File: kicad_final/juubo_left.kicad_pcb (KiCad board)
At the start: 2 copper layers, 145.6 x 125.5 mm, 42 parts

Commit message: Cleanup
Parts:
- removed REF** (x2): R_0201_0603, Resistor_SMD:R_0201_0603Metric_Pad0.64x0.40mm_HandSolder
- added DISP1: RES_ERJ2RKF4701X, RES_ERJ2RKF4701X, F.Cu at (209.5, 84.5)
- added DISP2: RES_ERJ2RKF4701X, RES_ERJ2RKF4701X, F.Cu at (207.6, 84.5)
- added JST1: , JST_PH_S2B-PH-K_02x2.00mm_Angled, F.Cu at (199.2, 91.1)
- added T1: , E73:SPDT_C128955, F.Cu at (199.2, 50.2)
- added _1: , MountingHole_2.2mm_M2_Pad_Via, F.Cu at (109.5, 67.6)
- added _2: , MountingHole_2.2mm_M2_Pad_Via, F.Cu at (166.7, 62.6)
- added _3: , MountingHole_2.2mm_M2_Pad_Via, F.Cu at (109.5, 105.7)
- added _4: , MountingHole_2.2mm_M2_Pad_Via, F.Cu at (177.9, 130.5)
- added _5: , MountingHole_2.2mm_M2_Pad_Via, F.Cu at (202.8, 149.3)
- added _6: , MountingHole_2.2mm_M2_Pad_Via, F.Cu at (166.7, 100.7)
- moved TRRS1 1.15 mm to (215.4, 91.7)
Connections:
- D1 pad 1: P16 -> P10
- D10 pad 1: P16 -> P10
- D11 pad 1: P14 -> P16
- D12 pad 1: P15 -> P14
- D13 pad 1: P16 -> P10
- D14 pad 1: P14 -> P16
- D15 pad 1: P15 -> P14
- D16 pad 1: P10 -> P6
- D17 pad 1: P10 -> P6
- D18 pad 1: P10 -> P6
- D2 pad 1: P14 -> P16
- D3 pad 1: P15 -> P14
- D4 pad 1: P16 -> P10
- D5 pad 1: P14 -> P16
- D6 pad 1: P15 -> P14
- D7 pad 1: P16 -> P10
- D8 pad 1: P14 -> P16
- D9 pad 1: P15 -> P14
- S1 pad 1: P18 -> P21
- S10 pad 1: P21 -> P18
- S11 pad 1: P21 -> P18
- S12 pad 1: P21 -> P18
- S13 pad 1: P1 -> P15
- S14 pad 1: P1 -> P15
- S15 pad 1: P1 -> P15
- S16 pad 1: P20 -> P19
- S17 pad 1: P21 -> P18
- S18 pad 1: P1 -> P15
- S2 pad 1: P18 -> P21
- S3 pad 1: P18 -> P21
- S4 pad 1: P19 -> P20
- S5 pad 1: P19 -> P20
- S6 pad 1: P19 -> P20
- S7 pad 1: P20 -> P19
- S8 pad 1: P20 -> P19
- S9 pad 1: P20 -> P19
- TRRS1 pad 2: P2 -> P3
- TRRS1 pad 3: P3 -> P2
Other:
- outline, holes or cut-outs redrawn
- net class Default added: clearance 0.2, trace_width 0.25, via_dia 0.8, via_drill 0.4

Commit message: Left routed
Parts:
- DISP1, DISP2: moved to B.Cu
- moved D5 11.8 mm to (107.4, 78.9)
- moved S9 11.8 mm to (126.5, 52.3)
- moved S14 11.8 mm to (164.6, 76.4)
- moved S17 11.8 mm to (184.2, 129.4)
- moved D11 11.8 mm to (145.5, 78.9)
- moved D9 11.8 mm to (126.5, 57.3)
- moved S5 11.8 mm to (107.4, 73.9)
- moved _6 11.8 mm to (155.0, 98.7)
- moved D1 11.8 mm to (88.4, 102.9)
- moved D8 11.8 mm to (126.5, 76.4)
- moved S7 11.8 mm to (126.5, 90.4)
- moved D6 11.8 mm to (107.4, 59.8)
- moved S2 11.8 mm to (88.4, 78.9)
- moved D10 11.8 mm to (145.5, 97.9)
- moved S18 11.8 mm to (201.9, 144.5)
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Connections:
- MCU1 pad 13: P1 -> VCC
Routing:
- net P15: track 0.00 -> 170.8 mm
- net P18: track 0.00 -> 170.4 mm
- net P19: track 0.00 -> 167.9 mm
- net P21: track 0.00 -> 155.2 mm
- net P10: track 0.00 -> 143.2 mm
- net P20: track 0.00 -> 136.0 mm
- net P14: track 0.00 -> 131.5 mm
- net P6: track 0.00 -> 128.9 mm
- net P16: track 0.00 -> 126.8 mm
- net GND: track 0.00 -> 116.9 mm
- net VCC: track 0.00 -> 60.1 mm, vias 0 -> 2
- net P2: track 0.00 -> 53.7 mm
- net P3: track 0.00 -> 43.1 mm
- net B+: track 0.00 -> 39.0 mm
- net RST: track 0.00 -> 33.0 mm
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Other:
- outline, holes or cut-outs redrawn
- net class Default removed

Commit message: Adjust and fix
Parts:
- moved T1 0.30 mm to (187.6, 48.4)
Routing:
- net RAW: track 5.66 -> 7.55 mm
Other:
- board size 145.6 x 125.5 mm -> 145.5 x 125.5 mm
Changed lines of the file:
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@@
   (net 40 "B+")
   (footprint "E73:SPDT_C128955" (layer "F.Cu")
-    (at 187.613786 48.115911)
+    (at 187.613786 48.4125)
     (attr through_hole)
     (fp_text reference "T1" (at 0 0) (layer "F.SilkS") hide
@@
       (net 36 "P2") (solder_mask_margin 0.102))
   )
-  (gr_arc (start 202.574223 162.941307) (mid 200.2 164) (end 197.676477 163.375839)
-    (stroke (width 0.15) (type solid)) (layer "Edge.Cuts"))
   (gr_arc (start 142.722221 109.098913) (mid 145.877217 110.612025) (end 146.634761 114.028112)
     (stroke (width 0.15) (type solid)) (layer "Edge.Cuts"))
@@
   (gr_arc (start 200.280578 47.697143) (mid 202.774498 48.99265) (end 203.800645 51.608921)
     (stroke (width 0.15) (type solid)) (layer "Edge.Cuts"))
+  (gr_line (start 202.748997 162.877717) (end 221.659673 144.499586)
+    (stroke (width 0.15) (type default)) (layer "Edge.Cuts"))
   (gr_arc (start 145.621497 129.763273) (mid 144.079016 127.892173) (end 143.900962 125.473809)
     (stroke (width 0.15) (type solid)) (layer "Edge.Cuts"))
-  (gr_arc (start 221.356718 139.908254) (mid 222.468094 142.788701) (end 221.197355 145.60246)
-    (stroke (width 0.15) (type solid)) (layer "Edge.Cuts"))
   (gr_line (start 76.838785 105.438871) (end 76.838784 51.396523)
-    (stroke (width 0.15) (type solid)) (layer "Edge.Cuts"))
-  (gr_line (start 221.197355 145.60246) (end 202.58661 162.953987)
     (stroke (width 0.15) (type solid)) (layer "Edge.Cuts"))
   (gr_line (start 79.823311 47.527571) (end 95.717823 43.355782)
@@
   (gr_line (start 143.900962 125.473809) (end 146.634761 114.028112)
     (stroke (width 0.15) (type solid)) (layer "Edge.Cuts"))
+  (gr_arc (start 202.748997 162.877717) (mid 200.311135 164.046527) (end 197.688861 163.388522)
+    (stroke (width 0.15) (type default)) (layer "Edge.Cuts"))
+  (gr_arc (start 221.356714 139.908256) (mid 222.292209 142.152188) (end 221.659673 144.499586)
+    (stroke (width 0.15) (type default)) (layer "Edge.Cuts"))
   (segment (start 191.023785 94.035912) (end 191.023785 83.040911) (width 0.25) (layer "F.Cu") (net 1))
   (segment (start 194.493785 97.505912) (end 191.023785 94.035912) (width 0.25) (layer "F.Cu") (net 1))
@@
   (segment (start 181.917187 124.803616) (end 181.404818 124.940904) (width 0.25) (layer "B.Cu") (net 31))
   (segment (start 153.589513 124.329439) (end 155.434623 125.001004) (width 0.25) (layer "B.Cu") (net 31))
+  (segment (start 181.6 51.6) (end 180.890909 50.890909) (width 0.25) (layer "B.Cu") (net 32))
+  (segment (start 185.363786 51.236214) (end 185 51.6) (width 0.25) (layer "B.Cu") (net 32))
+  (segment (start 180.890909 50.890909) (end 179.993787 50.890909) (width 0.25) (layer "B.Cu") (net 32))
   (segment (start 180.693785 50.190911) (end 179.993787 50.890909) (width 0.25) (layer "B.Cu") (net 32))
-  (segment (start 185.363786 50.190911) (end 180.693785 50.190911) (width 0.25) (layer "B.Cu") (net 32))
+  (segment (start 185 51.6) (end 181.6 51.6) (width 0.25) (layer "B.Cu") (net 32))
+  (segment (start 185.363786 50.4875) (end 185.363786 51.236214) (width 0.25) (layer "B.Cu") (net 32))
   (segment (start 202.141286 50.84591) (end 199.044757 47.749381) (width 0.25) (layer "F.Cu") (net 33))
   (segment (start 194.650619 47.749381) (end 186.429091 55.970909) (width 0.25) (layer "F.Cu") (net 33))
@@
   (segment (start 194.673785 88.548409) (end 196.8 88.548409) (width 0.25) (layer "B.Cu") (net 37))
   (segment (start 198.890909 63.590909) (end 195.233787 63.590909) (width 0.25) (layer "B.Cu") (net 37))
+  (segment (start 188.613785 89.063409) (end 188.613785 50.737499) (width 0.25) (layer "B.Cu") (net 40))
   (segment (start 188.613785 50.44091) (end 188.363786 50.190911) (width 0.25) (layer "B.Cu") (net 40))
-  (segment (start 188.613785 89.063409) (end 188.613785 50.44091) (width 0.25) (layer "B.Cu") (net 40))
+  (segment (start 188.613785 50.737499) (end 188.363786 50.4875) (width 0.25) (layer "B.Cu") (net 40))
 )

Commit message: random trash
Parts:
- DISP1, DISP2: moved to F.Cu
- moved D1 297.4 mm to (385.8, 105.0)
- moved S2 297.4 mm to (385.8, 81.0)
- moved D2 297.4 mm to (385.8, 86.0)
- moved S3 297.4 mm to (385.8, 61.9)
- moved D3 297.4 mm to (385.8, 66.9)
- moved S1 297.4 mm to (385.8, 100.0)
- moved _3 278.9 mm to (376.2, 86.7)
- moved _1 278.3 mm to (376.2, 67.6)
- moved D5 259.3 mm to (366.7, 81.0)
- moved S5 259.3 mm to (366.7, 76.0)
- moved D6 259.3 mm to (366.7, 61.9)
- moved S6 259.3 mm to (366.7, 56.9)
- moved S4 259.3 mm to (366.7, 95.0)
- moved D4 259.3 mm to (366.7, 100.0)
- moved S9 221.2 mm to (347.6, 54.4)
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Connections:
- net extra_cluster renamed mirror_extra_cluster
- net index_bottom renamed mirror_index_bottom
- net index_home renamed mirror_index_home
- net index_top renamed mirror_index_top
- net inner_bottom renamed mirror_inner_bottom
- net inner_home renamed mirror_inner_home
- net inner_top renamed mirror_inner_top
- net layer_cluster renamed mirror_layer_cluster
- net middle_bottom renamed mirror_middle_bottom
- net middle_home renamed mirror_middle_home
- net middle_top renamed mirror_middle_top
- net pinky_bottom renamed mirror_pinky_bottom
- net pinky_home renamed mirror_pinky_home
- net pinky_top renamed mirror_pinky_top
- net ring_bottom renamed mirror_ring_bottom
- net ring_home renamed mirror_ring_home
- net ring_top renamed mirror_ring_top
- net space_cluster renamed mirror_space_cluster
- D1 pad 1: P10 -> P16
- D10 pad 1: P10 -> P16
- D11 pad 1: P16 -> P14
- D12 pad 1: P14 -> P15
- D13 pad 1: P10 -> P16
- D14 pad 1: P16 -> P14
- D15 pad 1: P14 -> P15
- D16 pad 1: P6 -> P10
- D17 pad 1: P6 -> P10
- D18 pad 1: P6 -> P10
- D2 pad 1: P16 -> P14
- D3 pad 1: P14 -> P15
- D4 pad 1: P10 -> P16
- D5 pad 1: P16 -> P14
- D6 pad 1: P14 -> P15
- D7 pad 1: P10 -> P16
- D8 pad 1: P16 -> P14
- D9 pad 1: P14 -> P15
- MCU1 pad 13: VCC -> P1
- ROT1 pad 1: P9 -> P19
- ROT1 pad A: P7 -> P20
- ROT1 pad B: P8 -> P21
- S1 pad 1: P21 -> P4
- S10 pad 1: P18 -> P7
- S11 pad 1: P18 -> P7
- S12 pad 1: P18 -> P7
- S13 pad 1: P15 -> P8
- S14 pad 1: P15 -> P8
- S15 pad 1: P15 -> P8
- S16 pad 1: P19 -> P6
- S17 pad 1: P18 -> P7
- S18 pad 1: P15 -> P8
- S2 pad 1: P21 -> P4
- S3 pad 1: P21 -> P4
- S4 pad 1: P20 -> P5
- S5 pad 1: P20 -> P5
- S6 pad 1: P20 -> P5
- S7 pad 1: P19 -> P6
- S8 pad 1: P19 -> P6
- S9 pad 1: P19 -> P6
- TRRS1 pad 2: P3 -> P2
- TRRS1 pad 3: P2 -> P3
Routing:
- net P15: track 170.8 -> 0.00 mm
- net P18: track 170.4 -> 0.00 mm
- net P19: track 167.9 -> 0.00 mm
- net P21: track 155.2 -> 0.00 mm
- net P10: track 143.2 -> 0.00 mm
- net P20: track 136.0 -> 0.00 mm
- net P14: track 131.5 -> 0.00 mm
- net P6: track 128.9 -> 0.00 mm
- net P16: track 126.8 -> 0.00 mm
- net GND: track 116.9 -> 0.00 mm
- net VCC: track 60.1 -> 0.00 mm, vias 2 -> 0
- net P2: track 53.7 -> 0.00 mm
- net P3: track 43.1 -> 0.00 mm
- net B+: track 39.0 -> 0.00 mm
- net RST: track 33.0 -> 0.00 mm
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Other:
- board size 145.5 x 125.5 mm -> 145.6 x 125.5 mm
- net class Default added: clearance 0.2, trace_width 0.25, via_dia 0.8, via_drill 0.4

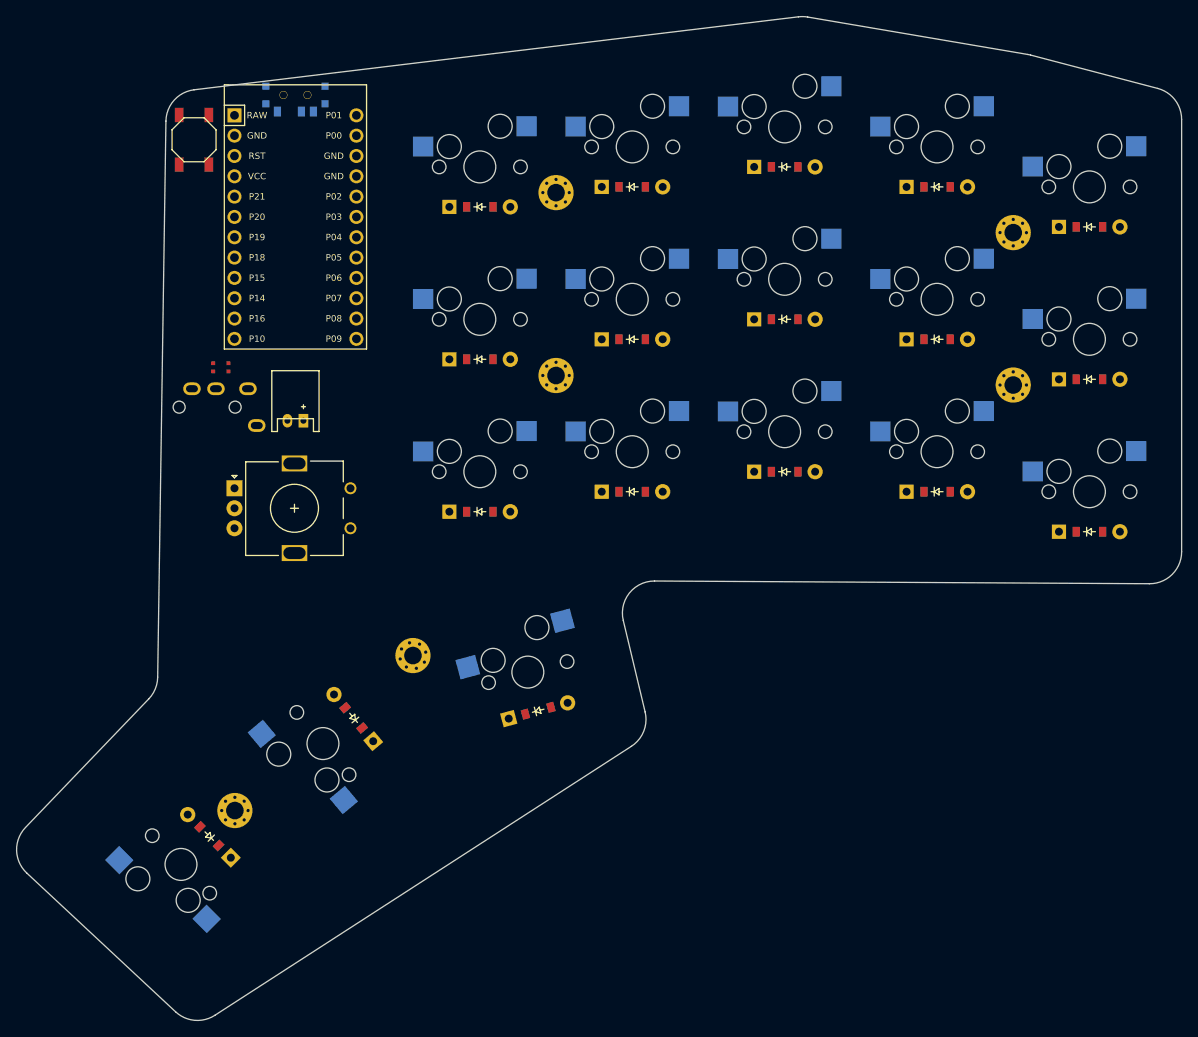
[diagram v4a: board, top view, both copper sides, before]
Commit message: Add qmk, gerber, kicad files
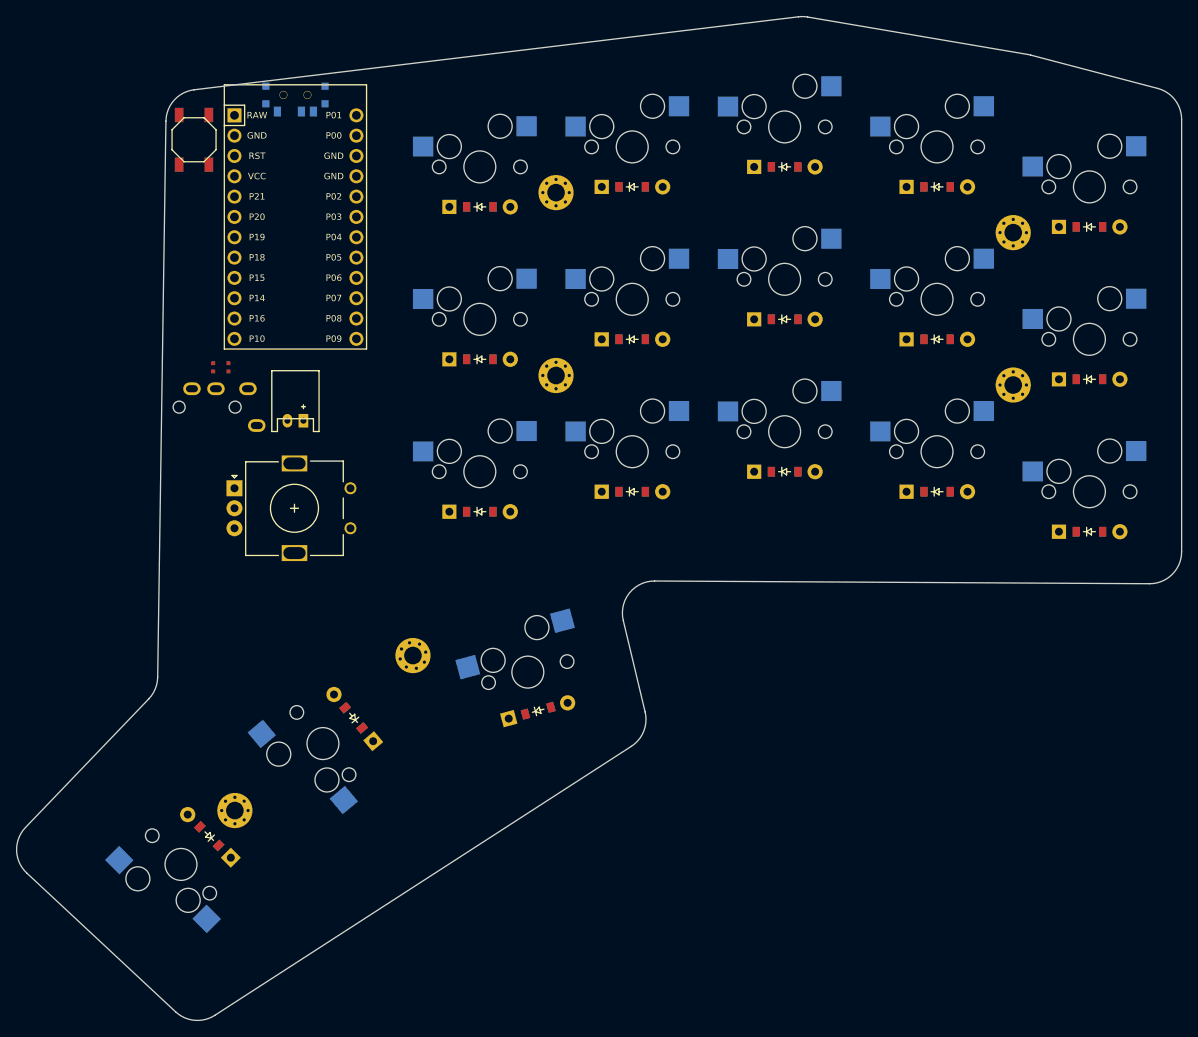
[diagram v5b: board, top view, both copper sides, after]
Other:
- net class Default removed
